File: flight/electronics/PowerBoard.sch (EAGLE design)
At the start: 13 parts, among them X1 JST-XH-02-PIN, X2 JST-XH-03-PIN, X3 JST-XH-03-PIN, X4 JST-XH-02-PIN, X6 JST-XH-03-PIN

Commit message: rev1 changes
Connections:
- net SWO: now also X2-3.S, X3-3.S, X4-2.S, X6-3.S
- net VBAT: no longer X2-3.S, X3-3.S, X4-2.S, X6-3.S
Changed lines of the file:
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@@
 <label x="142.24" y="129.54" size="1.778" layer="95" rot="R180" xref="yes"/>
-</segment>
-<segment>
-<pinref part="X4" gate="-2" pin="S"/>
-<wire x1="83.82" y1="38.1" x2="83.82" y2="25.4" width="0.1524" layer="91"/>
-<label x="83.82" y="25.4" size="1.778" layer="95" rot="R270" xref="yes"/>
-</segment>
-<segment>
-<pinref part="X2" gate="-3" pin="S"/>
-<wire x1="38.1" y1="38.1" x2="38.1" y2="35.56" width="0.1524" layer="91"/>
-<label x="38.1" y="35.56" size="1.778" layer="95" rot="R270" xref="yes"/>
-</segment>
-<segment>
-<wire x1="55.88" y1="38.1" x2="55.88" y2="35.56" width="0.1524" layer="91"/>
-<label x="55.88" y="35.56" size="1.778" layer="95" rot="R270" xref="yes"/>
-<pinref part="X3" gate="-3" pin="S"/>
-</segment>
-<segment>
-<wire x1="71.12" y1="38.1" x2="71.12" y2="35.56" width="0.1524" layer="91"/>
-<label x="71.12" y="35.56" size="1.778" layer="95" rot="R270" xref="yes"/>
-<pinref part="X6" gate="-3" pin="S"/>
 </segment>
 </net>
@@
 <pinref part="U$1" gate="G$1" pin="+VS"/>
 </segment>
+<segment>
+<pinref part="X2" gate="-3" pin="S"/>
+<wire x1="38.1" y1="38.1" x2="38.1" y2="35.56" width="0.1524" layer="91"/>
+<label x="38.1" y="35.56" size="1.778" layer="95" rot="R270" xref="yes"/>
+</segment>
+<segment>
+<wire x1="55.88" y1="38.1" x2="55.88" y2="35.56" width="0.1524" layer="91"/>
+<label x="55.88" y="35.56" size="1.778" layer="95" rot="R270" xref="yes"/>
+<pinref part="X3" gate="-3" pin="S"/>
+</segment>
+<segment>
+<wire x1="71.12" y1="38.1" x2="71.12" y2="35.56" width="0.1524" layer="91"/>
+<label x="71.12" y="35.56" size="1.778" layer="95" rot="R270" xref="yes"/>
+<pinref part="X6" gate="-3" pin="S"/>
+</segment>
+<segment>
+<pinref part="X4" gate="-2" pin="S"/>
+<wire x1="83.82" y1="38.1" x2="83.82" y2="25.4" width="0.1524" layer="91"/>
+<label x="83.82" y="25.4" size="1.778" layer="95" rot="R270" xref="yes"/>
+</segment>
 </net>

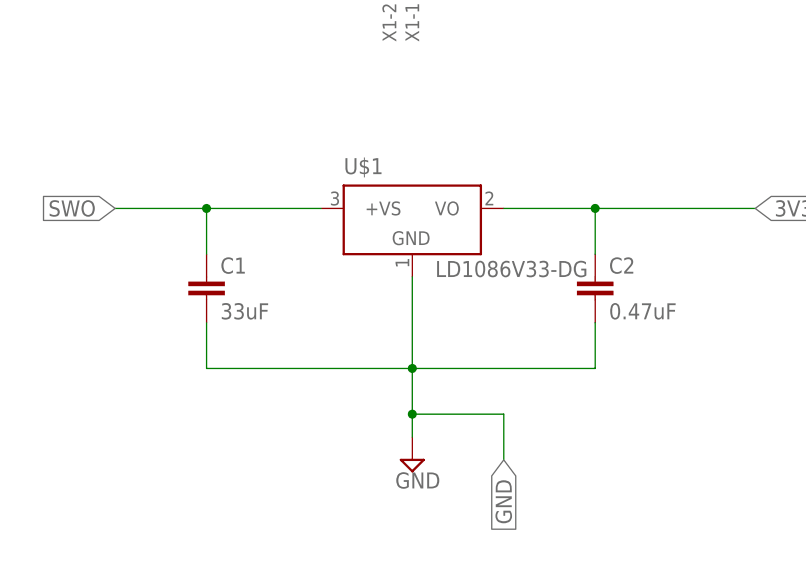
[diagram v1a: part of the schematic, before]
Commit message: update caps on pb
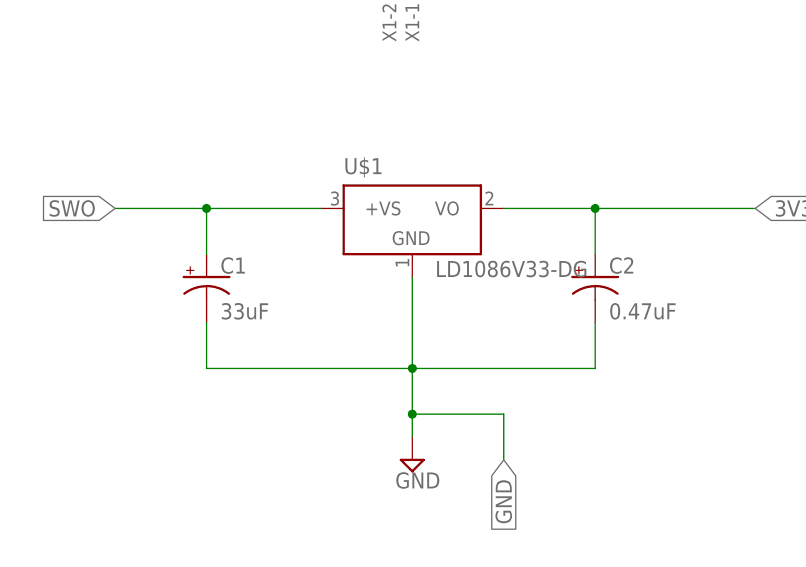
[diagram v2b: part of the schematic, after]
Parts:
- C1, C2: device capacitor-wima:C2,5-3 -> rcl:CPOL-USE2.5-5
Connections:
- net 3V3: now also C2.+; no longer C2.1
- net GND: now also C1.-, C2.-; no longer C1.2, C2.2
- net SWO: now also C1.+; no longer C1.1
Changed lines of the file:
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@@
 <parts>
 <part name="FRAME1" library="frames" library_urn="urn:adsk.eagle:library:229" deviceset="A4L-LOC" device=""/>
-<part name="C1" library="capacitor-wima" library_urn="urn:adsk.eagle:library:116" deviceset="C" device="2,5-3" package3d_urn="urn:adsk.eagle:package:5436/1" value="33uF"/>
-<part name="C2" library="capacitor-wima" library_urn="urn:adsk.eagle:library:116" deviceset="C" device="2,5-3" package3d_urn="urn:adsk.eagle:package:5436/1" value="0.47uF"/>
+<part name="C1" library="rcl" library_urn="urn:adsk.eagle:library:334" deviceset="CPOL-US" device="E2.5-5" package3d_urn="urn:adsk.eagle:package:23344/1" value="33uF"/>
+<part name="C2" library="rcl" library_urn="urn:adsk.eagle:library:334" deviceset="CPOL-US" device="E2.5-5" package3d_urn="urn:adsk.eagle:package:23344/1" value="0.47uF"/>
 <part name="SUPPLY1" library="supply2" library_urn="urn:adsk.eagle:library:372" deviceset="GND" device=""/>
 <part name="SUPPLY2" library="supply2" library_urn="urn:adsk.eagle:library:372" deviceset="GND" device=""/>
@@
 <wire x1="55.88" y1="96.52" x2="55.88" y2="86.36" width="0.1524" layer="91"/>
 <wire x1="55.88" y1="86.36" x2="33.02" y2="86.36" width="0.1524" layer="91"/>
-<pinref part="C1" gate="G$1" pin="2"/>
+<pinref part="C1" gate="G$1" pin="-"/>
 <wire x1="33.02" y1="86.36" x2="33.02" y2="91.44" width="0.1524" layer="91"/>
 <wire x1="55.88" y1="86.36" x2="76.2" y2="86.36" width="0.1524" layer="91"/>
 <junction x="55.88" y="86.36"/>
-<pinref part="C2" gate="G$1" pin="2"/>
+<pinref part="C2" gate="G$1" pin="-"/>
 <wire x1="76.2" y1="86.36" x2="76.2" y2="91.44" width="0.1524" layer="91"/>
 <pinref part="SUPPLY1" gate="GND" pin="GND"/>
@@
 </segment>
 <segment>
-<pinref part="C1" gate="G$1" pin="1"/>
+<pinref part="C1" gate="G$1" pin="+"/>
 <wire x1="33.02" y1="99.06" x2="33.02" y2="104.14" width="0.1524" layer="91"/>
 <wire x1="33.02" y1="104.14" x2="22.86" y2="104.14" width="0.1524" layer="91"/>
@@
 </segment>
 <segment>
-<pinref part="C2" gate="G$1" pin="1"/>
+<pinref part="C2" gate="G$1" pin="+"/>
 <wire x1="76.2" y1="99.06" x2="76.2" y2="104.14" width="0.1524" layer="91"/>
 <wire x1="76.2" y1="104.14" x2="66.04" y2="104.14" width="0.1524" layer="91"/>
@@
 packages will not be understood (or retained) with this version.
 </note>
+<note version="8.4" severity="warning">
+Since Version 8.4, EAGLE supports properties for SPICE simulation.
+Probes in schematics and SPICE mapping objects found in parts and library devices
+will not be understood with this version. Update EAGLE to the latest version
+for full support of SPICE simulation.
+</note>
 </compatibility>
